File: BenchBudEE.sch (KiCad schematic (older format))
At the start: 0 parts

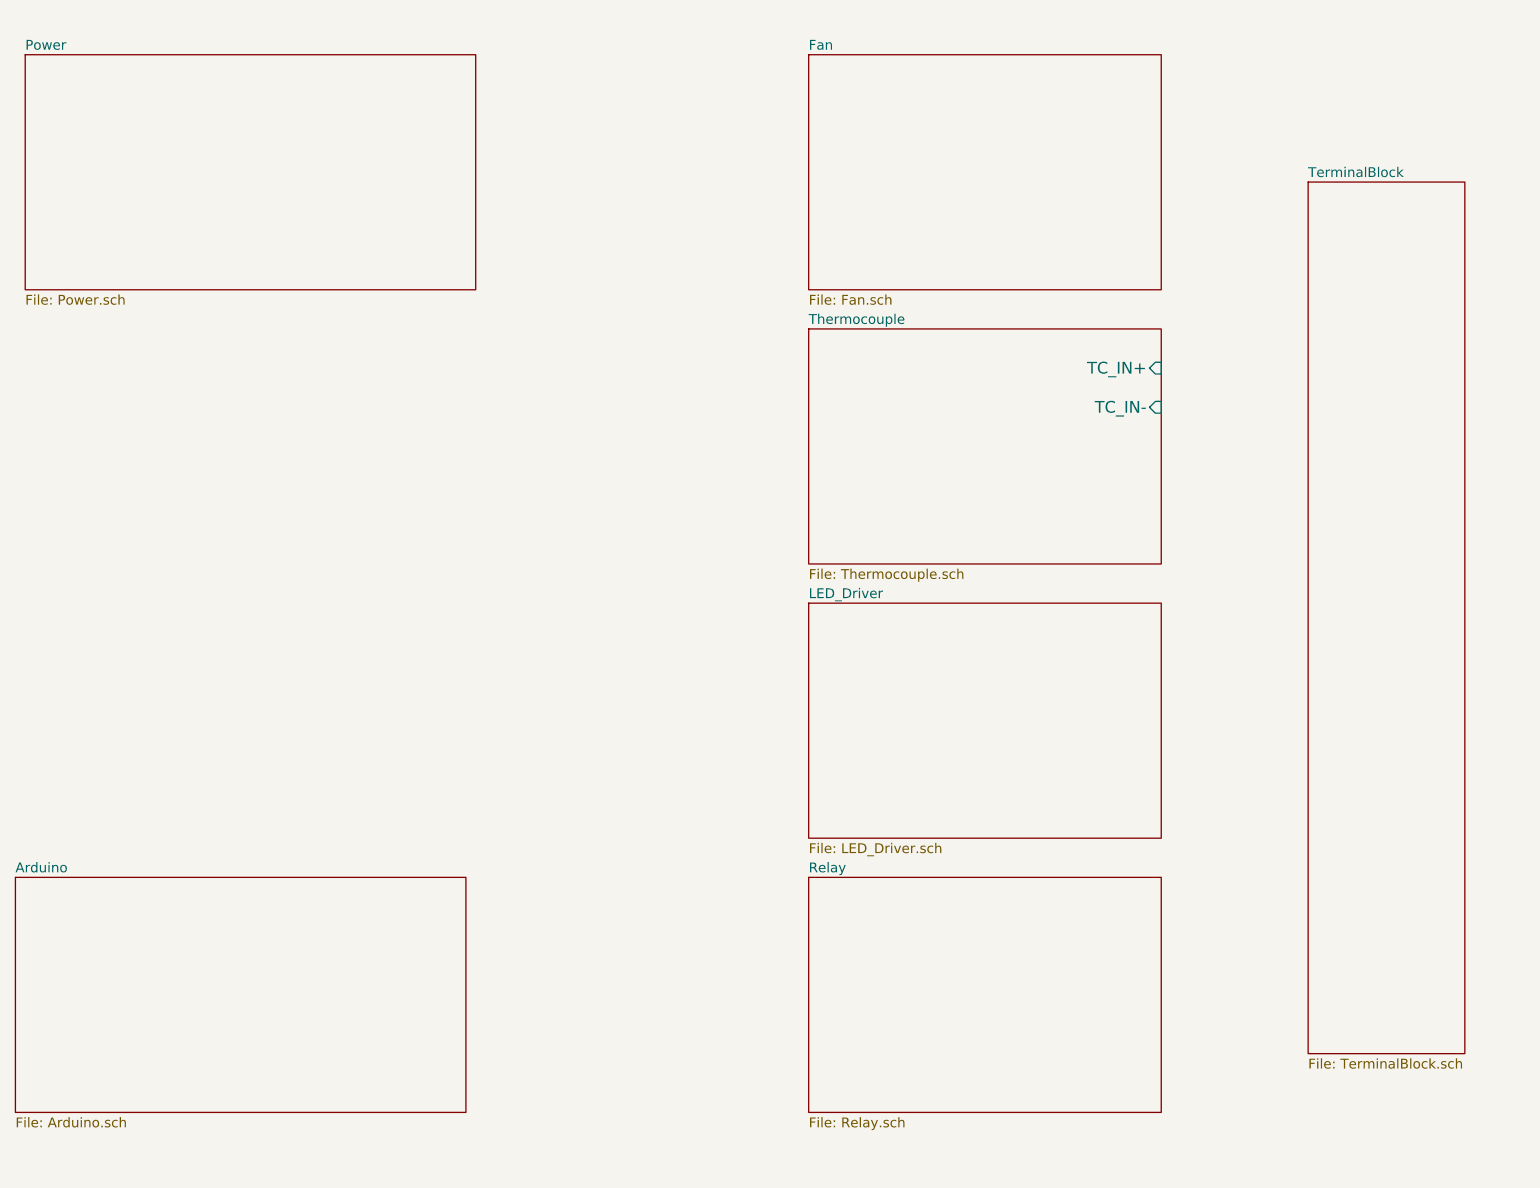
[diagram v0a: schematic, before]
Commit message: Inputs/outputs added to hierarchical schematics
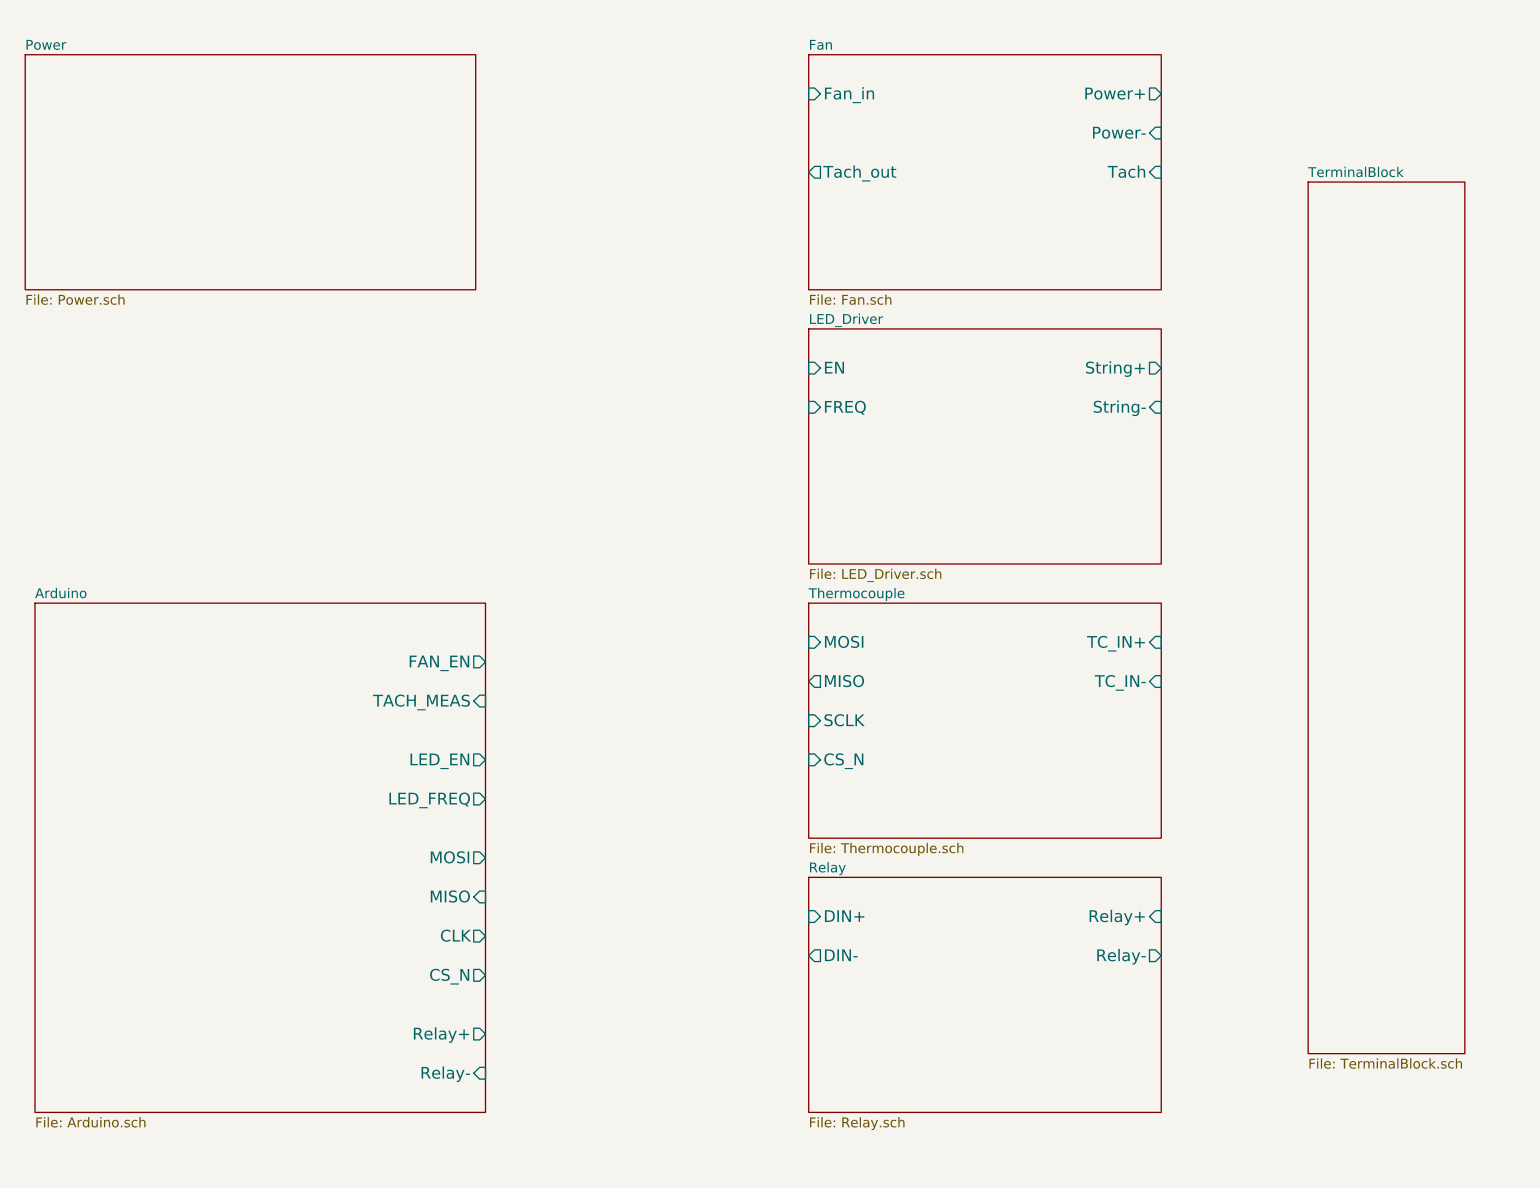
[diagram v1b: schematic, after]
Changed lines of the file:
@@
 $EndDescr
 $Sheet
-S 3450 5000 2300 1200
-U 52EAE42B
-F0 "Arduino" 50
-F1 "Arduino.sch" 50
-$EndSheet
-$Sheet
-S 7500 2200 1800 1200
+S 7500 3600 1800 1200
 U 52EAE493
 F0 "Thermocouple" 50
 F1 "Thermocouple.sch" 50
-F2 "TC_IN+" I R 9300 2400 60
-F3 "TC_IN-" I R 9300 2600 60
+F2 "TC_IN+" I R 9300 3800 60
+F3 "TC_IN-" I R 9300 4000 60
+F4 "MOSI" I L 7500 3800 60
+F5 "MISO" O L 7500 4000 60
+F6 "SCLK" I L 7500 4200 60
+F7 "CS_N" I L 7500 4400 60
 $EndSheet
 $Sheet
@@
 F0 "Relay" 50
 F1 "Relay.sch" 50
+F2 "DIN+" I L 7500 5200 60
+F3 "DIN-" O L 7500 5400 60
+F4 "Relay+" I R 9300 5200 60
+F5 "Relay-" O R 9300 5400 60
 $EndSheet
 $Sheet
-S 7500 3600 1800 1200
+S 7500 2200 1800 1200
 U 52EAE512
 F0 "LED_Driver" 50
 F1 "LED_Driver.sch" 50
-$EndSheet
-$Sheet
-S 7500 800  1800 1200
-U 52EAE52A
-F0 "Fan" 50
-F1 "Fan.sch" 50
+F2 "EN" I L 7500 2400 60
+F3 "FREQ" I L 7500 2600 60
+F4 "String+" O R 9300 2400 60
+F5 "String-" I R 9300 2600 60
 $EndSheet
 $Sheet
@@
 F1 "TerminalBlock.sch" 50
 $EndSheet
+$Sheet
+S 7500 800  1800 1200
+U 52EAE52A
+F0 "Fan" 50
+F1 "Fan.sch" 50
+F2 "Power+" O R 9300 1000 60
+F3 "Power-" I R 9300 1200 60
+F4 "Tach" I R 9300 1400 60
+F5 "Tach_out" O L 7500 1400 60
+F6 "Fan_in" I L 7500 1000 60
+$EndSheet
+$Sheet
+S 3550 3600 2300 2600
+U 52EAE42B
+F0 "Arduino" 50
+F1 "Arduino.sch" 50
+F2 "Relay+" O R 5850 5800 60
+F3 "Relay-" I R 5850 6000 60
+F4 "MOSI" O R 5850 4900 60
+F5 "MISO" I R 5850 5100 60
+F6 "CLK" O R 5850 5300 60
+F7 "CS_N" O R 5850 5500 60
+F8 "LED_EN" O R 5850 4400 60
+F9 "LED_FREQ" O R 5850 4600 60
+F10 "FAN_EN" O R 5850 3900 60
+F11 "TACH_MEAS" I R 5850 4100 60
+$EndSheet
 $EndSCHEMATC

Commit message: Rough schematic created for fan driver circuit
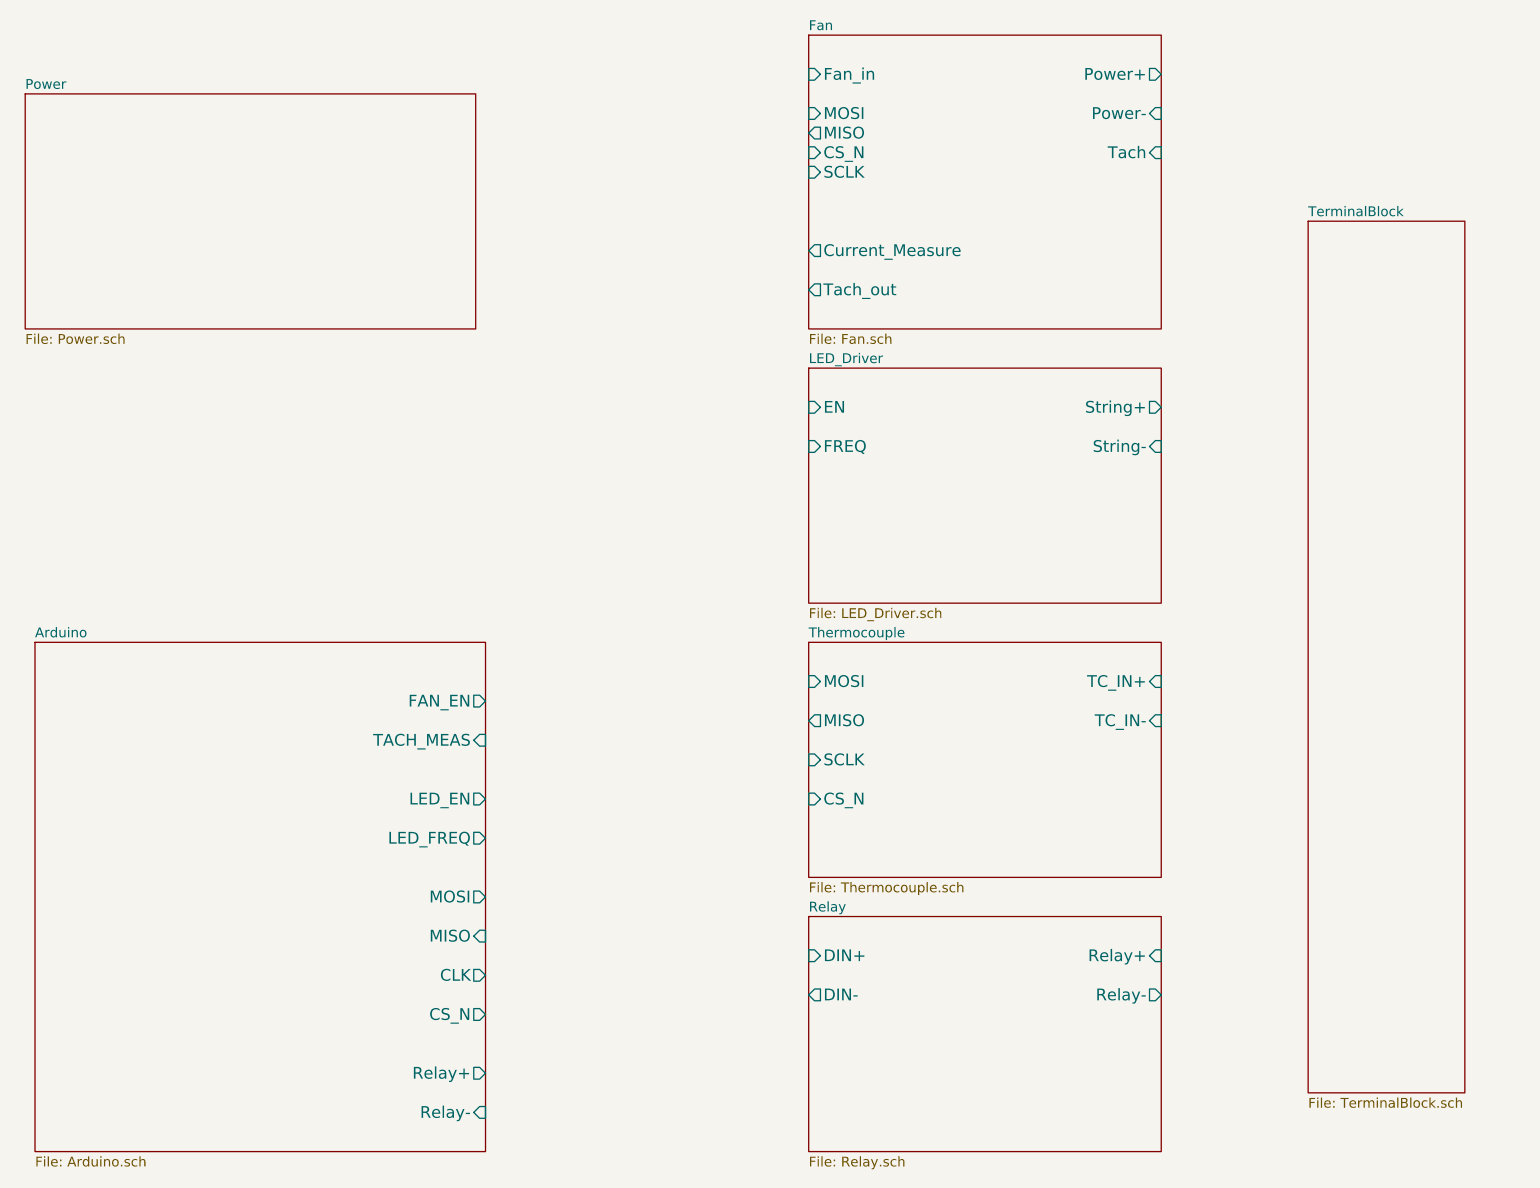
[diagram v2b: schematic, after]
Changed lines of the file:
@@
 $EndDescr
 $Sheet
-S 7500 3600 1800 1200
+S 7500 3800 1800 1200
 U 52EAE493
 F0 "Thermocouple" 50
 F1 "Thermocouple.sch" 50
-F2 "TC_IN+" I R 9300 3800 60
-F3 "TC_IN-" I R 9300 4000 60
-F4 "MOSI" I L 7500 3800 60
-F5 "MISO" O L 7500 4000 60
-F6 "SCLK" I L 7500 4200 60
-F7 "CS_N" I L 7500 4400 60
+F2 "TC_IN+" I R 9300 4000 60
+F3 "TC_IN-" I R 9300 4200 60
+F4 "MOSI" I L 7500 4000 60
+F5 "MISO" O L 7500 4200 60
+F6 "SCLK" I L 7500 4400 60
+F7 "CS_N" I L 7500 4600 60
 $EndSheet
 $Sheet
-S 7500 5000 1800 1200
+S 7500 5200 1800 1200
 U 52EAE4BD
 F0 "Relay" 50
 F1 "Relay.sch" 50
-F2 "DIN+" I L 7500 5200 60
-F3 "DIN-" O L 7500 5400 60
-F4 "Relay+" I R 9300 5200 60
-F5 "Relay-" O R 9300 5400 60
+F2 "DIN+" I L 7500 5400 60
+F3 "DIN-" O L 7500 5600 60
+F4 "Relay+" I R 9300 5400 60
+F5 "Relay-" O R 9300 5600 60
 $EndSheet
 $Sheet
-S 7500 2200 1800 1200
+S 7500 2400 1800 1200
 U 52EAE512
 F0 "LED_Driver" 50
 F1 "LED_Driver.sch" 50
-F2 "EN" I L 7500 2400 60
-F3 "FREQ" I L 7500 2600 60
-F4 "String+" O R 9300 2400 60
-F5 "String-" I R 9300 2600 60
+F2 "EN" I L 7500 2600 60
+F3 "FREQ" I L 7500 2800 60
+F4 "String+" O R 9300 2600 60
+F5 "String-" I R 9300 2800 60
 $EndSheet
 $Sheet
-S 3500 800  2300 1200
+S 3500 1000 2300 1200
 U 52EAE4E0
 F0 "Power" 50
@@
 $EndSheet
 $Sheet
-S 10050 1450 800  4450
+S 10050 1650 800  4450
 U 52EAE551
 F0 "TerminalBlock" 50
@@
 $EndSheet
 $Sheet
-S 7500 800  1800 1200
+S 7500 700  1800 1500
 U 52EAE52A
 F0 "Fan" 50
 F1 "Fan.sch" 50
-F2 "Power+" O R 9300 1000 60
-F3 "Power-" I R 9300 1200 60
-F4 "Tach" I R 9300 1400 60
-F5 "Tach_out" O L 7500 1400 60
-F6 "Fan_in" I L 7500 1000 60
+F2 "Power+" O R 9300 900 60
+F3 "Power-" I R 9300 1100 60
+F4 "Tach" I R 9300 1300 60
+F5 "Tach_out" O L 7500 2000 60
+F6 "Fan_in" I L 7500 900 60
+F7 "Current_Measure" O L 7500 1800 60
+F8 "MOSI" I L 7500 1100 60
+F9 "MISO" O L 7500 1200 60
+F10 "CS_N" I L 7500 1300 60
+F11 "SCLK" I L 7500 1400 60
 $EndSheet
 $Sheet
-S 3550 3600 2300 2600
+S 3550 3800 2300 2600
 U 52EAE42B
 F0 "Arduino" 50
 F1 "Arduino.sch" 50
-F2 "Relay+" O R 5850 5800 60
-F3 "Relay-" I R 5850 6000 60
-F4 "MOSI" O R 5850 4900 60
-F5 "MISO" I R 5850 5100 60
-F6 "CLK" O R 5850 5300 60
-F7 "CS_N" O R 5850 5500 60
-F8 "LED_EN" O R 5850 4400 60
-F9 "LED_FREQ" O R 5850 4600 60
-F10 "FAN_EN" O R 5850 3900 60
-F11 "TACH_MEAS" I R 5850 4100 60
+F2 "Relay+" O R 5850 6000 60
+F3 "Relay-" I R 5850 6200 60
+F4 "MOSI" O R 5850 5100 60
+F5 "MISO" I R 5850 5300 60
+F6 "CLK" O R 5850 5500 60
+F7 "CS_N" O R 5850 5700 60
+F8 "LED_EN" O R 5850 4600 60
+F9 "LED_FREQ" O R 5850 4800 60
+F10 "FAN_EN" O R 5850 4100 60
+F11 "TACH_MEAS" I R 5850 4300 60
 $EndSheet
 $EndSCHEMATC
